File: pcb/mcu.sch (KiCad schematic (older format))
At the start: 10 parts, among them U1 STM32F103C8Tx, Y1 Crystal

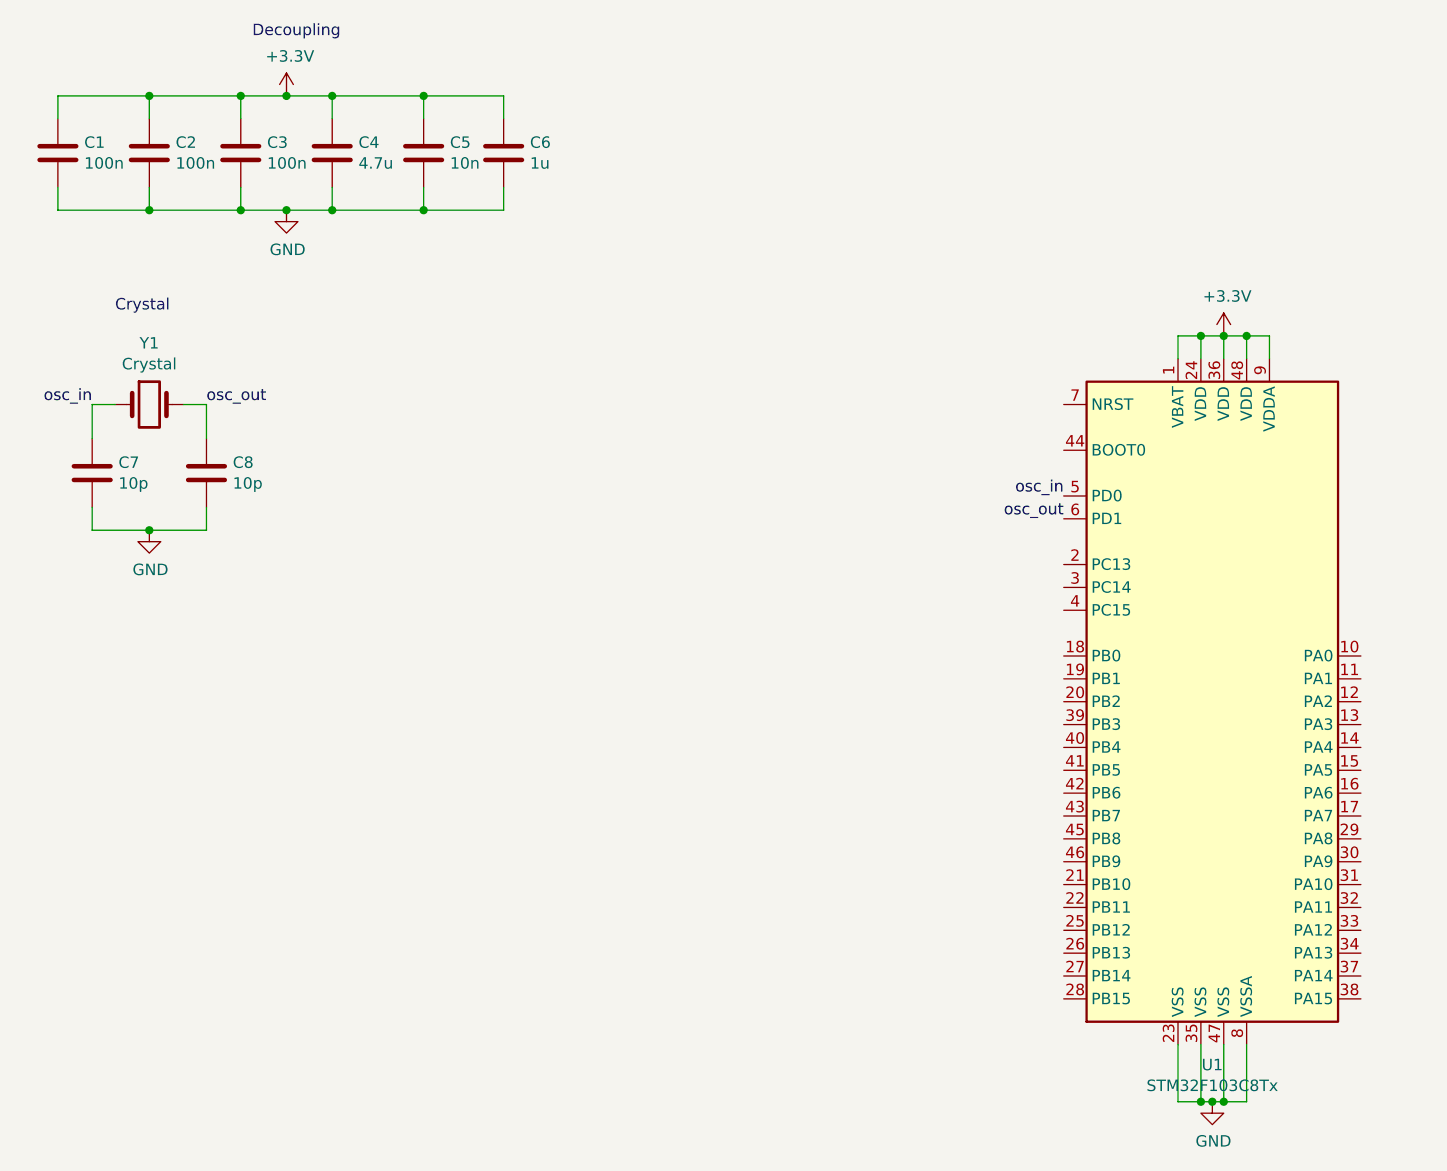
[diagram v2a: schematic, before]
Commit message: [PCB & Firmware] SWD Interface
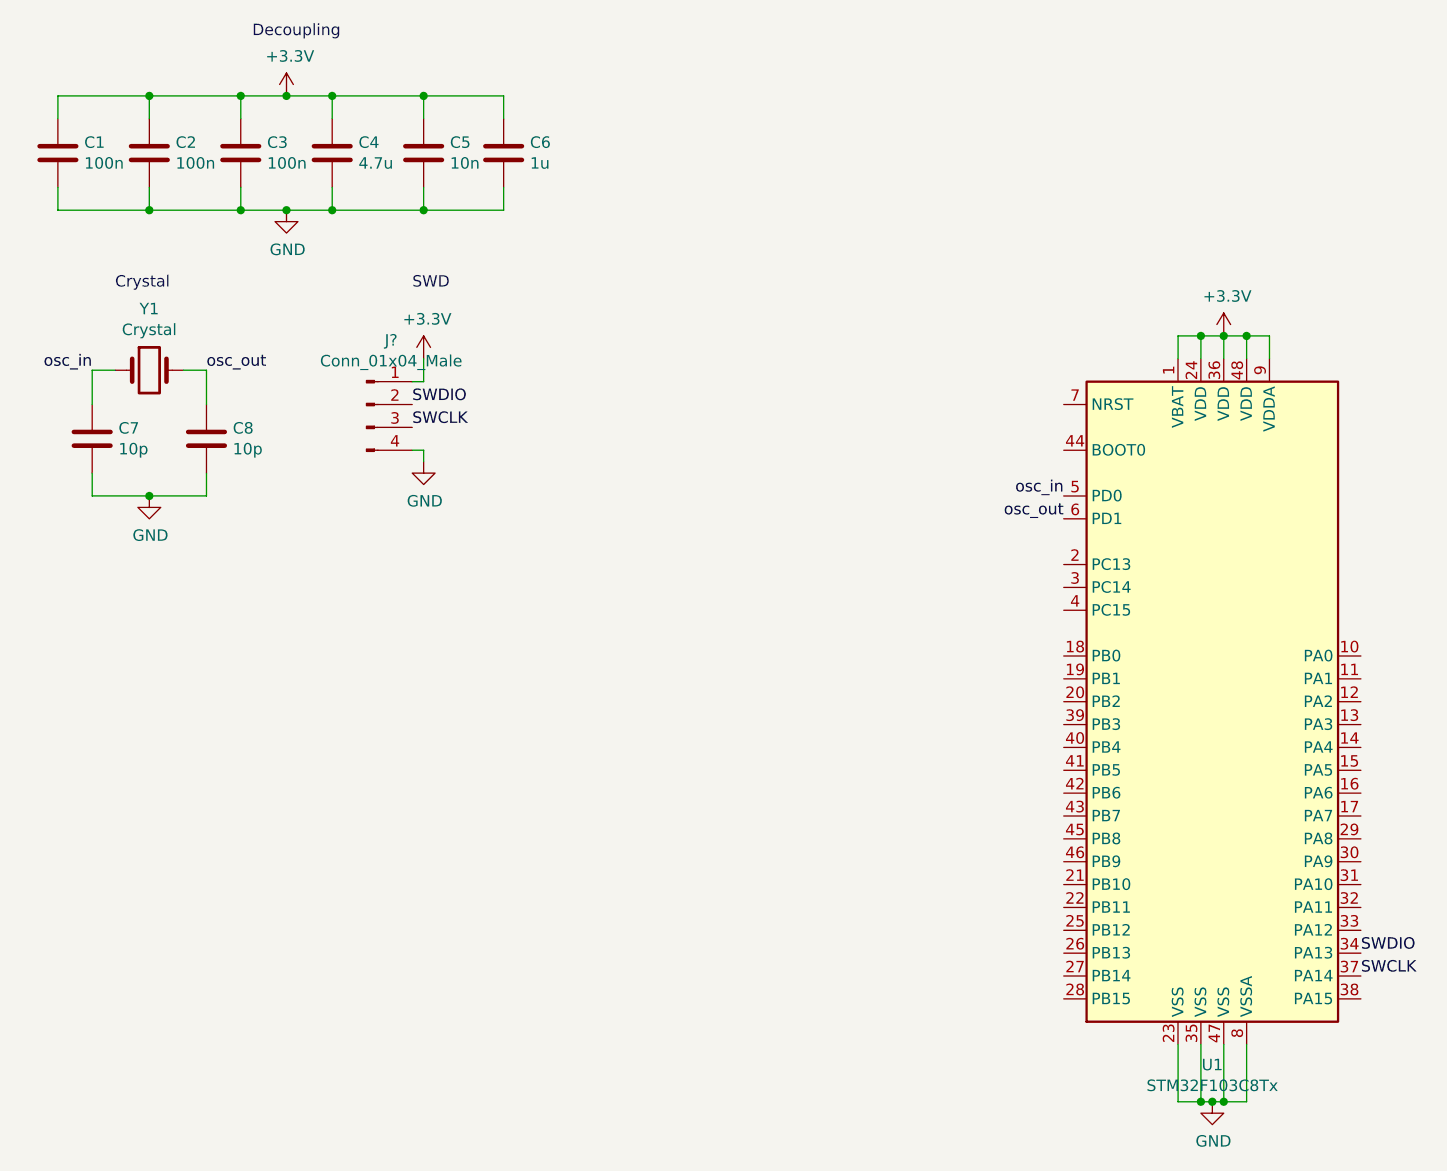
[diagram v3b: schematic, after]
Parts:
- added J?: Conn_01x04_Male, symbol Connector:Conn_01x04_Male
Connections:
- net +3V3: now also J?.1 (Pin_1)
- net GND: now also J?.4 (Pin_4)
- net SWDIO: now reaches U1.34 (PA13)
- net SWDIO: now also J?.2 (Pin_2)
- net SWCLK: now reaches U1.37 (PA14)
- net SWCLK: now also J?.3 (Pin_3)
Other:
- note added: "SWD"
- moved on the sheet: C7, C8, Y1
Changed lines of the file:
@@
 EESchema Schematic File Version 4
+LIBS:rasbot-cache
 EELAYER 29 0
 EELAYER END
@@
 Wire Wire Line
 	1850 1350 2250 1350
-Text Notes 900  1800 0    50   ~ 0
+Text Notes 900  1700 0    50   ~ 0
 Crystal
 $Comp
 L Device:Crystal Y1
 U 1 1 5D0DE5C2
-P 1050 2200
-F 0 "Y1" H 1050 2468 50  0000 C CNN
-F 1 "Crystal" H 1050 2377 50  0000 C CNN
-F 2 "Crystal:Crystal_SMD_HC49-SD" H 1050 2200 50  0001 C CNN
-F 3 "~" H 1050 2200 50  0001 C CNN
-	1    1050 2200
+P 1050 2050
+F 0 "Y1" H 1050 2318 50  0000 C CNN
+F 1 "Crystal" H 1050 2227 50  0000 C CNN
+F 2 "Crystal:Crystal_SMD_HC49-SD" H 1050 2050 50  0001 C CNN
+F 3 "~" H 1050 2050 50  0001 C CNN
+	1    1050 2050
 	1    0    0    -1
 $EndComp
@@
 L power:GND #PWR04
 U 1 1 5D0DEFF9
-P 1050 2750
-F 0 "#PWR04" H 1050 2500 50  0001 C CNN
-F 1 "GND" H 1055 2577 50  0000 C CNN
-F 2 "" H 1050 2750 50  0001 C CNN
-F 3 "" H 1050 2750 50  0001 C CNN
-	1    1050 2750
+P 1050 2600
+F 0 "#PWR04" H 1050 2350 50  0001 C CNN
+F 1 "GND" H 1055 2427 50  0000 C CNN
+F 2 "" H 1050 2600 50  0001 C CNN
+F 3 "" H 1050 2600 50  0001 C CNN
+	1    1050 2600
 	1    0    0    -1
 $EndComp
@@
 L Device:C C7
 U 1 1 5D0DF7DE
-P 800 2500
-F 0 "C7" H 915 2546 50  0000 L CNN
-F 1 "10p" H 915 2455 50  0000 L CNN
-F 2 "Capacitor_SMD:C_0805_2012Metric" H 838 2350 50  0001 C CNN
-F 3 "~" H 800 2500 50  0001 C CNN
-	1    800  2500
+P 800 2350
+F 0 "C7" H 915 2396 50  0000 L CNN
+F 1 "10p" H 915 2305 50  0000 L CNN
+F 2 "Capacitor_SMD:C_0805_2012Metric" H 838 2200 50  0001 C CNN
+F 3 "~" H 800 2350 50  0001 C CNN
+	1    800  2350
 	1    0    0    -1
 $EndComp
@@
 L Device:C C8
 U 1 1 5D0DFE7A
-P 1300 2500
-F 0 "C8" H 1415 2546 50  0000 L CNN
-F 1 "10p" H 1415 2455 50  0000 L CNN
-F 2 "Capacitor_SMD:C_0805_2012Metric" H 1338 2350 50  0001 C CNN
-F 3 "~" H 1300 2500 50  0001 C CNN
-	1    1300 2500
-	1    0    0    -1
-$EndComp
-Wire Wire Line
-	800  2650 800  2750
-Wire Wire Line
-	800  2750 1050 2750
-Wire Wire Line
-	1300 2650 1300 2750
-Wire Wire Line
-	1300 2750 1050 2750
-Connection ~ 1050 2750
-Wire Wire Line
-	800  2350 800  2200
-Wire Wire Line
-	800  2200 900  2200
-Wire Wire Line
-	1200 2200 1300 2200
-Wire Wire Line
-	1300 2200 1300 2350
-Text Label 800  2200 2    50   ~ 0
+P 1300 2350
+F 0 "C8" H 1415 2396 50  0000 L CNN
+F 1 "10p" H 1415 2305 50  0000 L CNN
+F 2 "Capacitor_SMD:C_0805_2012Metric" H 1338 2200 50  0001 C CNN
+F 3 "~" H 1300 2350 50  0001 C CNN
+	1    1300 2350
+	1    0    0    -1
+$EndComp
+Wire Wire Line
+	800  2500 800  2600
+Wire Wire Line
+	800  2600 1050 2600
+Wire Wire Line
+	1300 2500 1300 2600
+Wire Wire Line
+	1300 2600 1050 2600
+Connection ~ 1050 2600
+Wire Wire Line
+	800  2200 800  2050
+Wire Wire Line
+	800  2050 900  2050
+Wire Wire Line
+	1200 2050 1300 2050
+Wire Wire Line
+	1300 2050 1300 2200
+Text Label 800  2050 2    50   ~ 0
 osc_in
-Text Label 1300 2200 0    50   ~ 0
+Text Label 1300 2050 0    50   ~ 0
 osc_out
 Text Label 5050 2600 2    50   ~ 0
@@
 Text Label 5050 2700 2    50   ~ 0
 osc_out
+Text Notes 2200 1700 0    50   ~ 0
+SWD
+$Comp
+L Connector:Conn_01x04_Male J?
+U 1 1 5D0B2068
+P 2000 2200
+F 0 "J?" H 2108 2481 50  0000 C CNN
+F 1 "Conn_01x04_Male" H 2108 2390 50  0000 C CNN
+F 2 "" H 2000 2200 50  0001 C CNN
+F 3 "~" H 2000 2200 50  0001 C CNN
+	1    2000 2200
+	1    0    0    -1
+$EndComp
+$Comp
+L power:GND #PWR?
+U 1 1 5D0B3FE0
+P 2250 2450
+F 0 "#PWR?" H 2250 2200 50  0001 C CNN
+F 1 "GND" H 2255 2277 50  0000 C CNN
+F 2 "" H 2250 2450 50  0001 C CNN
+F 3 "" H 2250 2450 50  0001 C CNN
+	1    2250 2450
+	1    0    0    -1
+$EndComp
+Wire Wire Line
+	2250 2450 2250 2400
+Wire Wire Line
+	2250 2400 2200 2400
+$Comp
+L power:+3.3V #PWR?
+U 1 1 5D0B53BA
+P 2250 2000
+F 0 "#PWR?" H 2250 1850 50  0001 C CNN
+F 1 "+3.3V" H 2265 2173 50  0000 C CNN
+F 2 "" H 2250 2000 50  0001 C CNN
+F 3 "" H 2250 2000 50  0001 C CNN
+	1    2250 2000
+	1    0    0    -1
+$EndComp
+Wire Wire Line
+	2250 2000 2250 2100
+Wire Wire Line
+	2250 2100 2200 2100
+Text Label 2200 2200 0    50   ~ 0
+SWDIO
+Text Label 2200 2300 0    50   ~ 0
+SWCLK
+Text Label 6350 4600 0    50   ~ 0
+SWDIO
+Text Label 6350 4700 0    50   ~ 0
+SWCLK
 $EndSCHEMATC

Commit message: [PCB] Reset Button, Power LED, BOOT pins and LSE Crystal
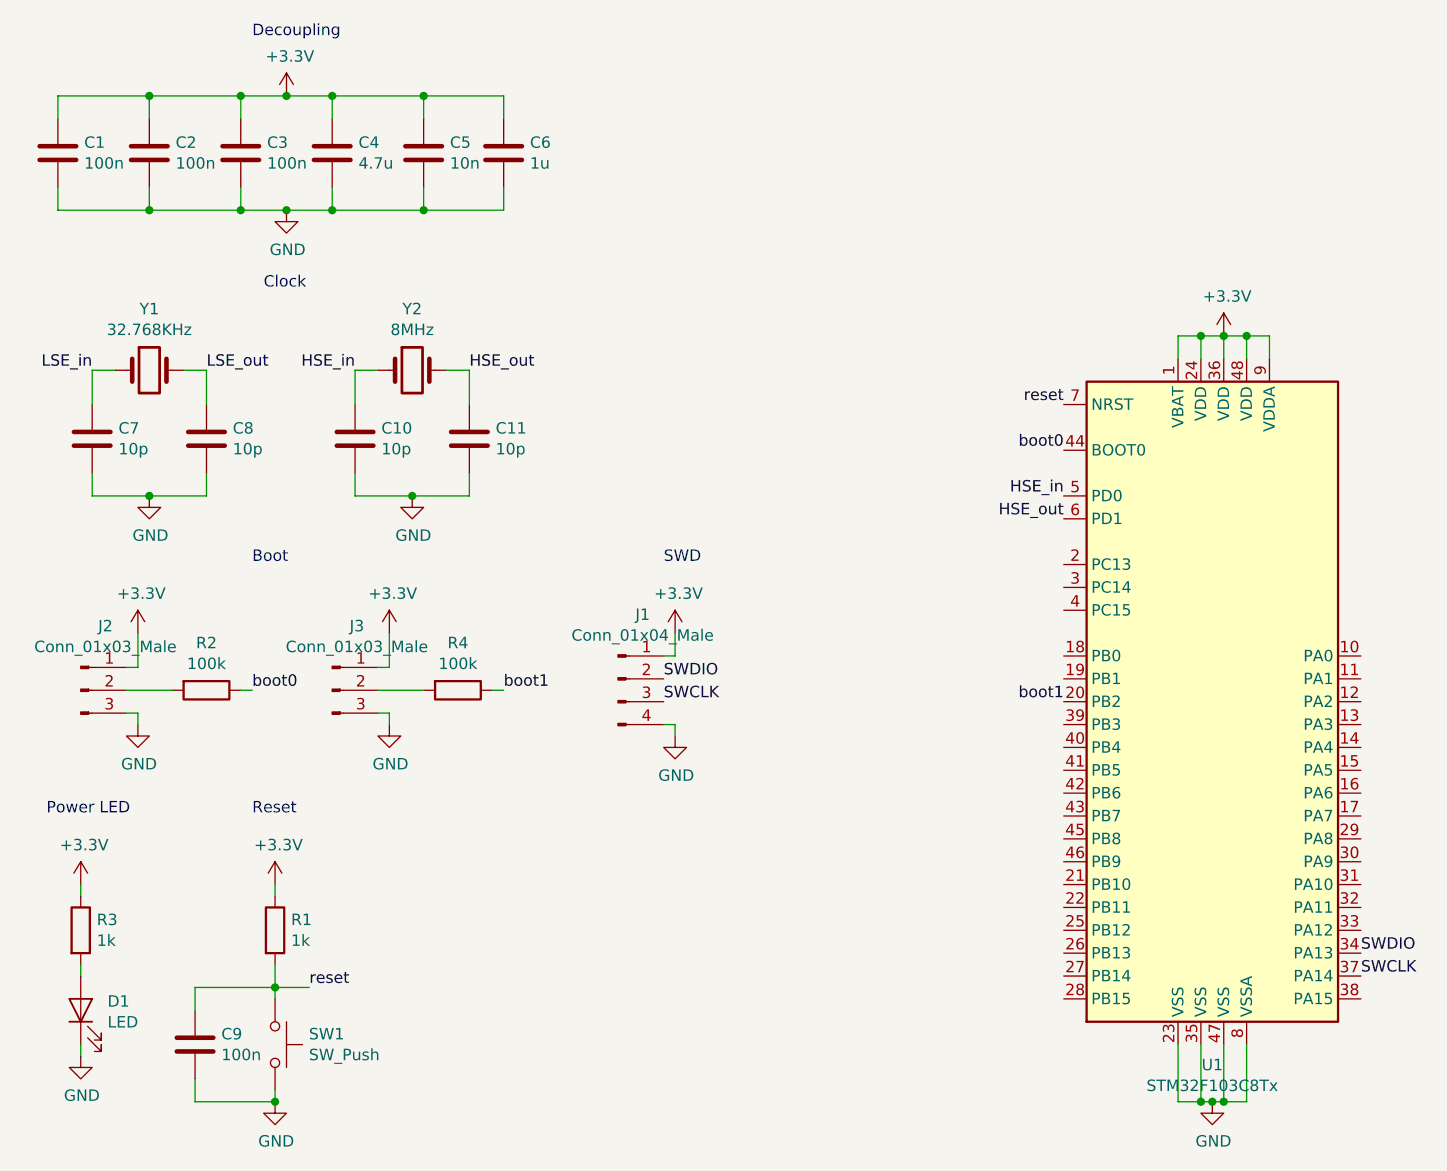
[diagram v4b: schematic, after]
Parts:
- added C10, C11: 10p, Capacitor_SMD:C_0805_2012Metric, symbol Device:C
- added C9: 100n, Capacitor_SMD:C_0805_2012Metric, symbol Device:C
- added D1: LED, Diode_SMD:D_0805_2012Metric, symbol Device:LED
- added J2, J3: Conn_01x03_Male, Connector_PinHeader_2.54mm:PinHeader_1x03_P2.54mm_Vertical, symbol Connector:Conn_01x03_Male
- added R1, R3: 1k, Resistor_SMD:R_0805_2012Metric, symbol Device:R
- added R2, R4: 100k, Resistor_SMD:R_0805_2012Metric, symbol Device:R
- added SW1: SW_Push, symbol Switch:SW_Push
- added Y2: 8MHz, Crystal:Crystal_SMD_HC49-SD, symbol Device:Crystal
- Y1: value Crystal -> 32.768KHz; footprint Crystal:Crystal_SMD_HC49-SD -> Crystal:Crystal_SMD_SeikoEpson_MC306-4Pin_8.0x3.2mm
- gave numbers to parts that had none: 1
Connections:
- net +3V3: now also J2.1 (Pin_1), J3.1 (Pin_1), R1.1, R3.1
- net GND: now also C10.2, C11.2, C9.2, D1.1 (K), J2.3 (Pin_3), J3.3 (Pin_3), SW1.2
- net boot1: now reaches U1.20 (PB2)
- net boot1: now also R4.1
- net boot0: now reaches U1.44 (BOOT0)
- net boot0: now also R2.1
- net reset: now reaches U1.7 (NRST)
- net reset: now also C9.1, R1.2, SW1.1
- net osc_in renamed LSE_in
- net LSE_in: no longer U1.5 (PD0)
- net osc_out renamed LSE_out
- net LSE_out: no longer U1.6 (PD1)
- new net: J2.2 (Pin_2), R2.2
- new net: D1.2 (A), R3.2
- new net: J3.2 (Pin_2), R4.2
- new net HSE_in: C10.1, U1.5 (PD0), Y2.1
- new net HSE_out: C11.1, U1.6 (PD1), Y2.2
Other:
- note added: "Boot\n"
- note added: "Clock"
- note added: "Power LED"
- note added: "Reset"
- note removed: "Crystal"
- moved on the sheet: J1

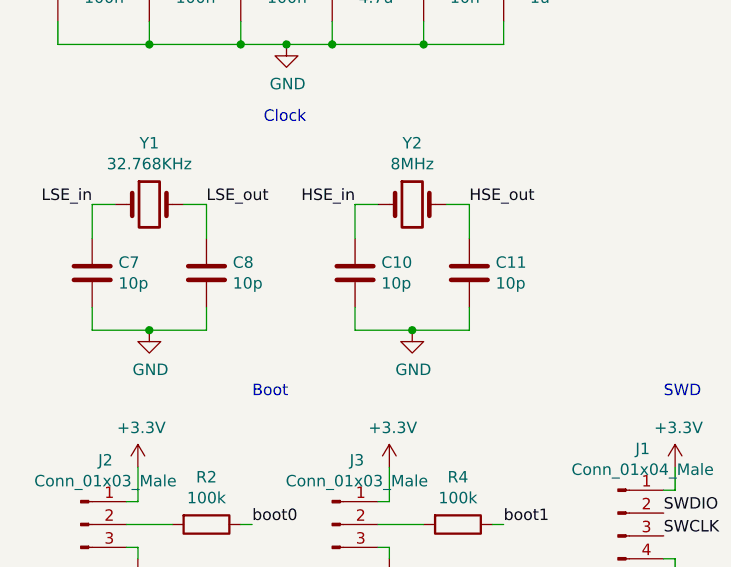
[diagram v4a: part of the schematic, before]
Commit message: [PCB] Crystal Capacitor Sizing
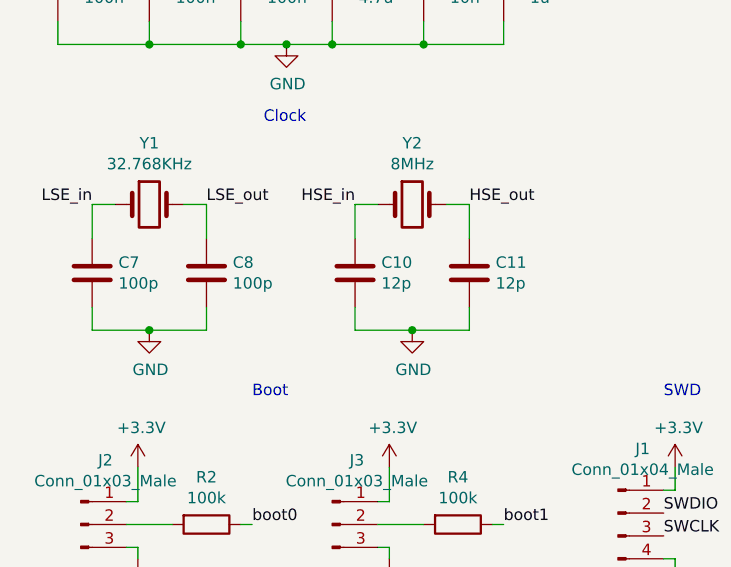
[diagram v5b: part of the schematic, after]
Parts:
- C10, C11: value 10p -> 12p
- C7, C8: value 10p -> 100p
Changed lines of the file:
@@
 P 800 2350
 F 0 "C7" H 915 2396 50  0000 L CNN
-F 1 "10p" H 915 2305 50  0000 L CNN
+F 1 "100p" H 915 2305 50  0000 L CNN
 F 2 "Capacitor_SMD:C_0805_2012Metric" H 838 2200 50  0001 C CNN
 F 3 "~" H 800 2350 50  0001 C CNN
@@
 P 1300 2350
 F 0 "C8" H 1415 2396 50  0000 L CNN
-F 1 "10p" H 1415 2305 50  0000 L CNN
+F 1 "100p" H 1415 2305 50  0000 L CNN
 F 2 "Capacitor_SMD:C_0805_2012Metric" H 1338 2200 50  0001 C CNN
 F 3 "~" H 1300 2350 50  0001 C CNN
@@
 P 1950 2350
 F 0 "C10" H 2065 2396 50  0000 L CNN
-F 1 "10p" H 2065 2305 50  0000 L CNN
+F 1 "12p" H 2065 2305 50  0000 L CNN
 F 2 "Capacitor_SMD:C_0805_2012Metric" H 1988 2200 50  0001 C CNN
 F 3 "~" H 1950 2350 50  0001 C CNN
@@
 P 2450 2350
 F 0 "C11" H 2565 2396 50  0000 L CNN
-F 1 "10p" H 2565 2305 50  0000 L CNN
+F 1 "12p" H 2565 2305 50  0000 L CNN
 F 2 "Capacitor_SMD:C_0805_2012Metric" H 2488 2200 50  0001 C CNN
 F 3 "~" H 2450 2350 50  0001 C CNN

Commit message: [PCB & Firmware] SWD Connector and Reset Button Footprint and Firmware LSE Enable
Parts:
- J1: footprint (none) -> Connector_PinHeader_2.54mm:PinHeader_1x04_P2.54mm_Vertical
- SW1: footprint (none) -> Button_Switch_SMD:SW_SPST_CK_RS282G05A3
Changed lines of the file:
@@
 F 0 "SW1" V 1554 5148 50  0000 L CNN
 F 1 "SW_Push" V 1645 5148 50  0000 L CNN
-F 2 "" H 1600 5200 50  0001 C CNN
+F 2 "Button_Switch_SMD:SW_SPST_CK_RS282G05A3" H 1600 5200 50  0001 C CNN
 F 3 "~" H 1600 5200 50  0001 C CNN
 	1    1600 5000
@@
 F 0 "J1" H 3208 3681 50  0000 C CNN
 F 1 "Conn_01x04_Male" H 3208 3590 50  0000 C CNN
-F 2 "" H 3100 3400 50  0001 C CNN
+F 2 "Connector_PinHeader_2.54mm:PinHeader_1x04_P2.54mm_Vertical" H 3100 3400 50  0001 C CNN
 F 3 "~" H 3100 3400 50  0001 C CNN
 	1    3100 3400
